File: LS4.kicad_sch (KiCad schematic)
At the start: 9 parts, among them U10 VNLD5160TR-E, U11 VNLD5160TR-E, U14 VNLD5160TR-E

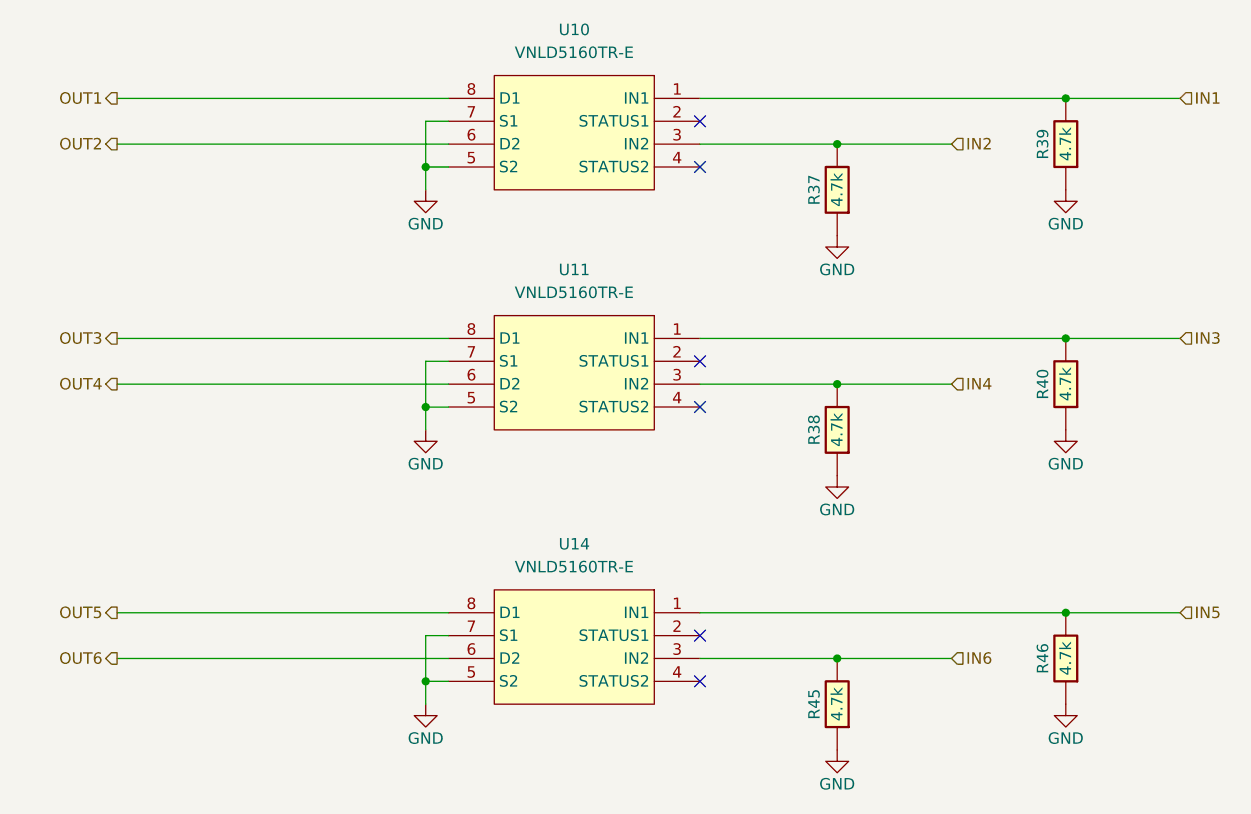
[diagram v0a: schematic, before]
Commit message: Standalone version without hellen-one
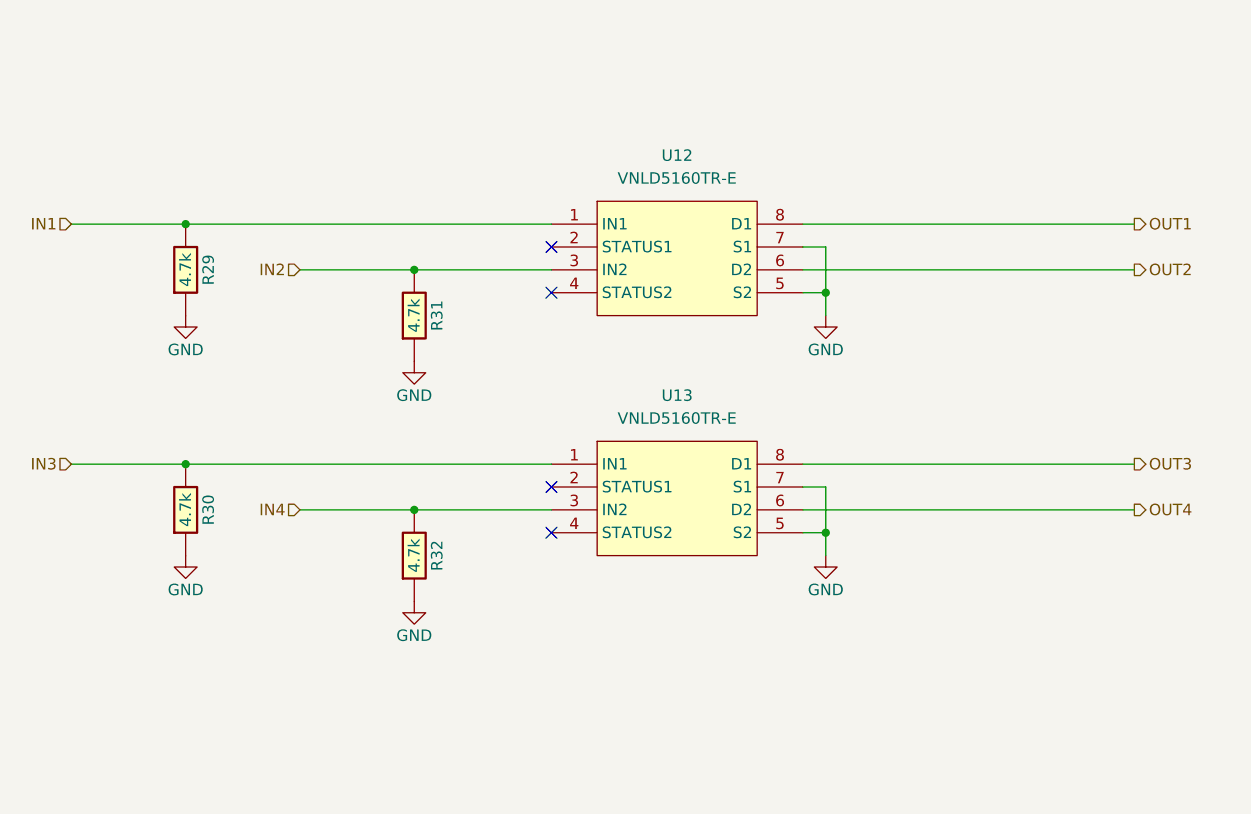
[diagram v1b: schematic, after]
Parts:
- removed R45, R46: 4.7k, hellen-one-common:R0603, symbol hellen-one-common:Res
- removed U14: VNLD5160TR-E, Package_SO:SOIC-8_3.9x4.9mm_P1.27mm, symbol chips:VNLD5160
- R29: renamed from R39; footprint hellen-one-common:R0603 -> Resistor_SMD:R_0603_1608Metric
- R30: renamed from R40; footprint hellen-one-common:R0603 -> Resistor_SMD:R_0603_1608Metric
- R31: renamed from R37; footprint hellen-one-common:R0603 -> Resistor_SMD:R_0603_1608Metric
- R32: renamed from R38; footprint hellen-one-common:R0603 -> Resistor_SMD:R_0603_1608Metric
- renumbered U10 to U12, U11 to U13
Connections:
- no-connect marks 6 -> 4
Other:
- moved on the sheet: R29, R30, R31, R32, U12, U13
